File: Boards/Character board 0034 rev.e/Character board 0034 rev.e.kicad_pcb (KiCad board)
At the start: 2 copper layers, 166.4 x 186.7 mm, 40 parts, among them J1 card edge, J2 character connector, J3 power jumper, J4 return jumper, Q1 TIP130A, U1 2.2K, U11 ULN2003A, U12 ULN2003A, U13 7406, U2 2.2K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

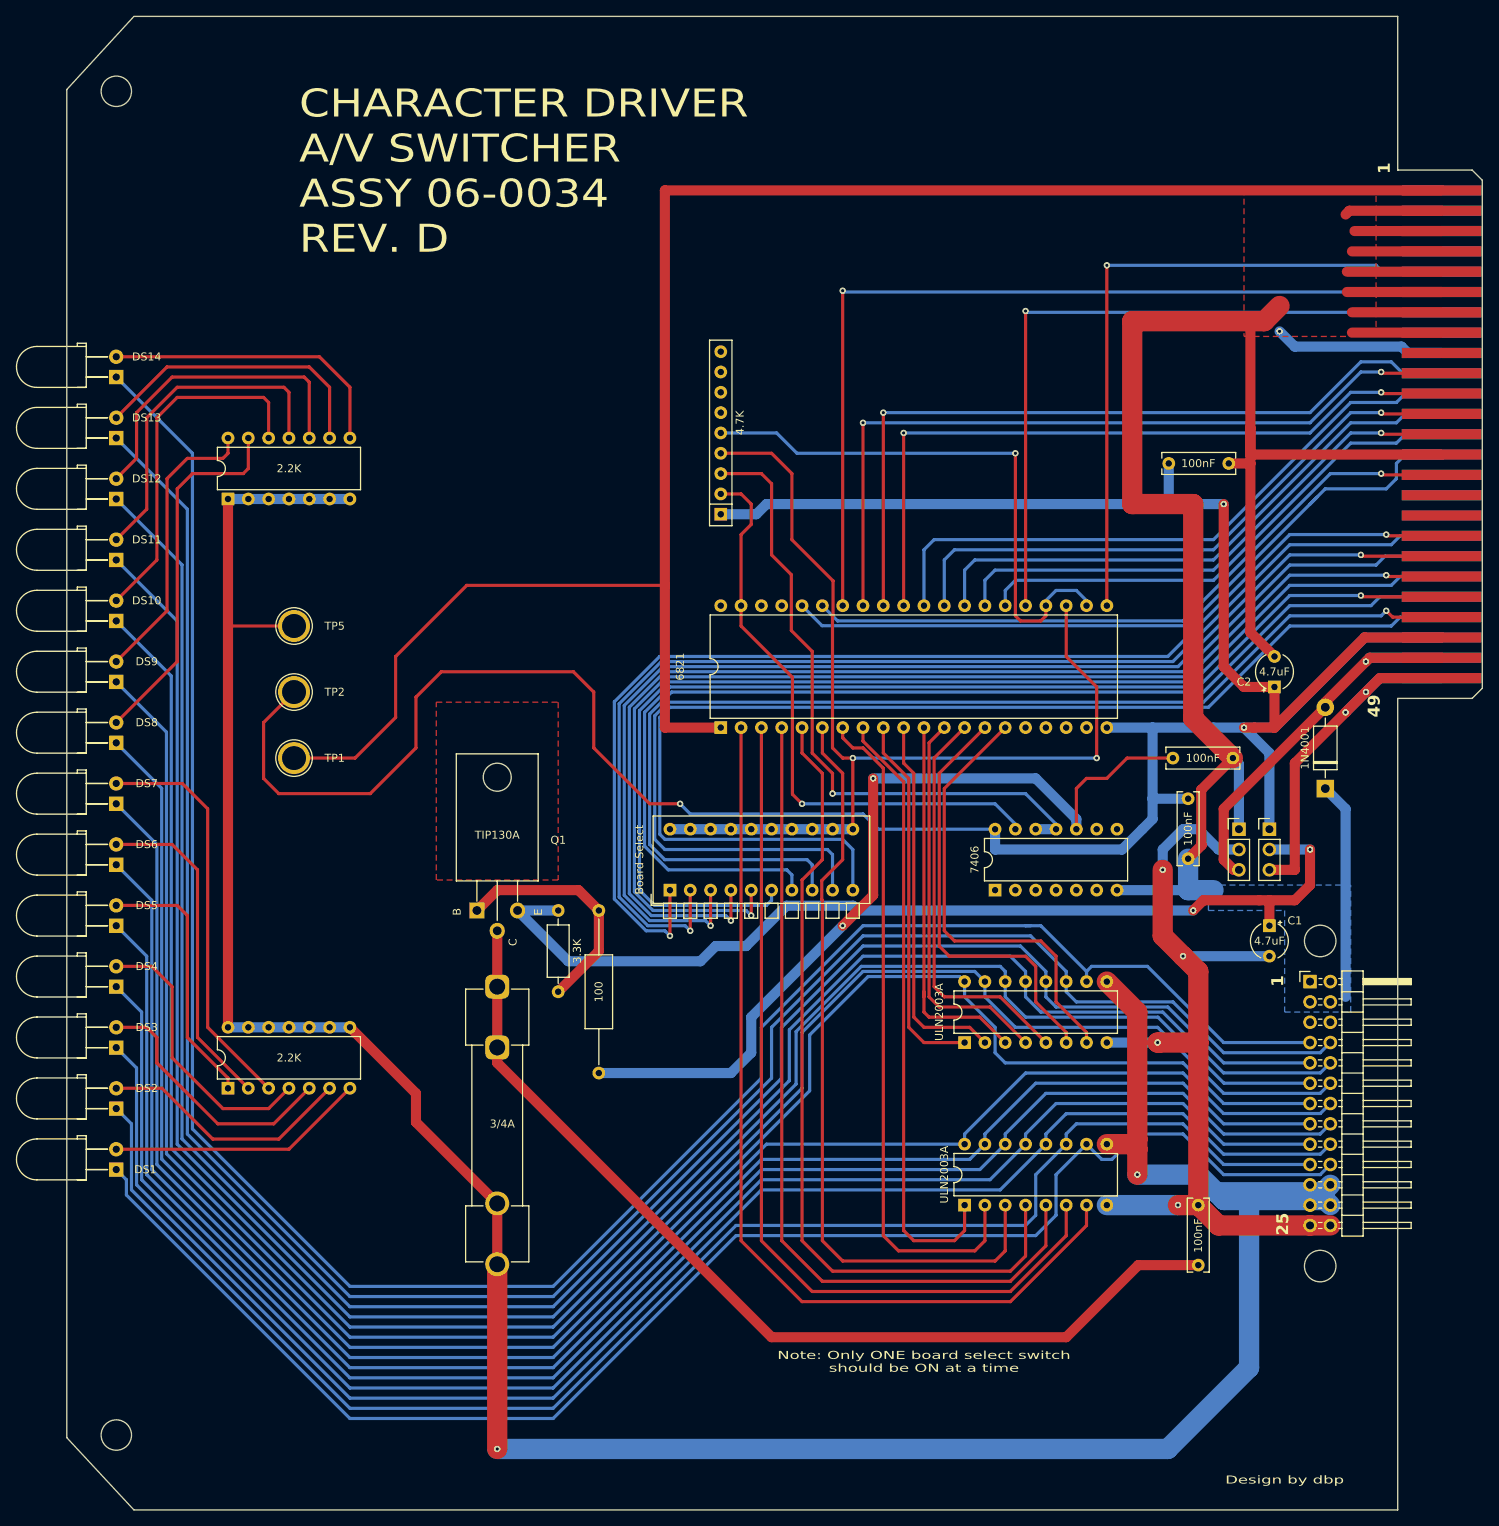
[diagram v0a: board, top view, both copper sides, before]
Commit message: renamed files and started the light card
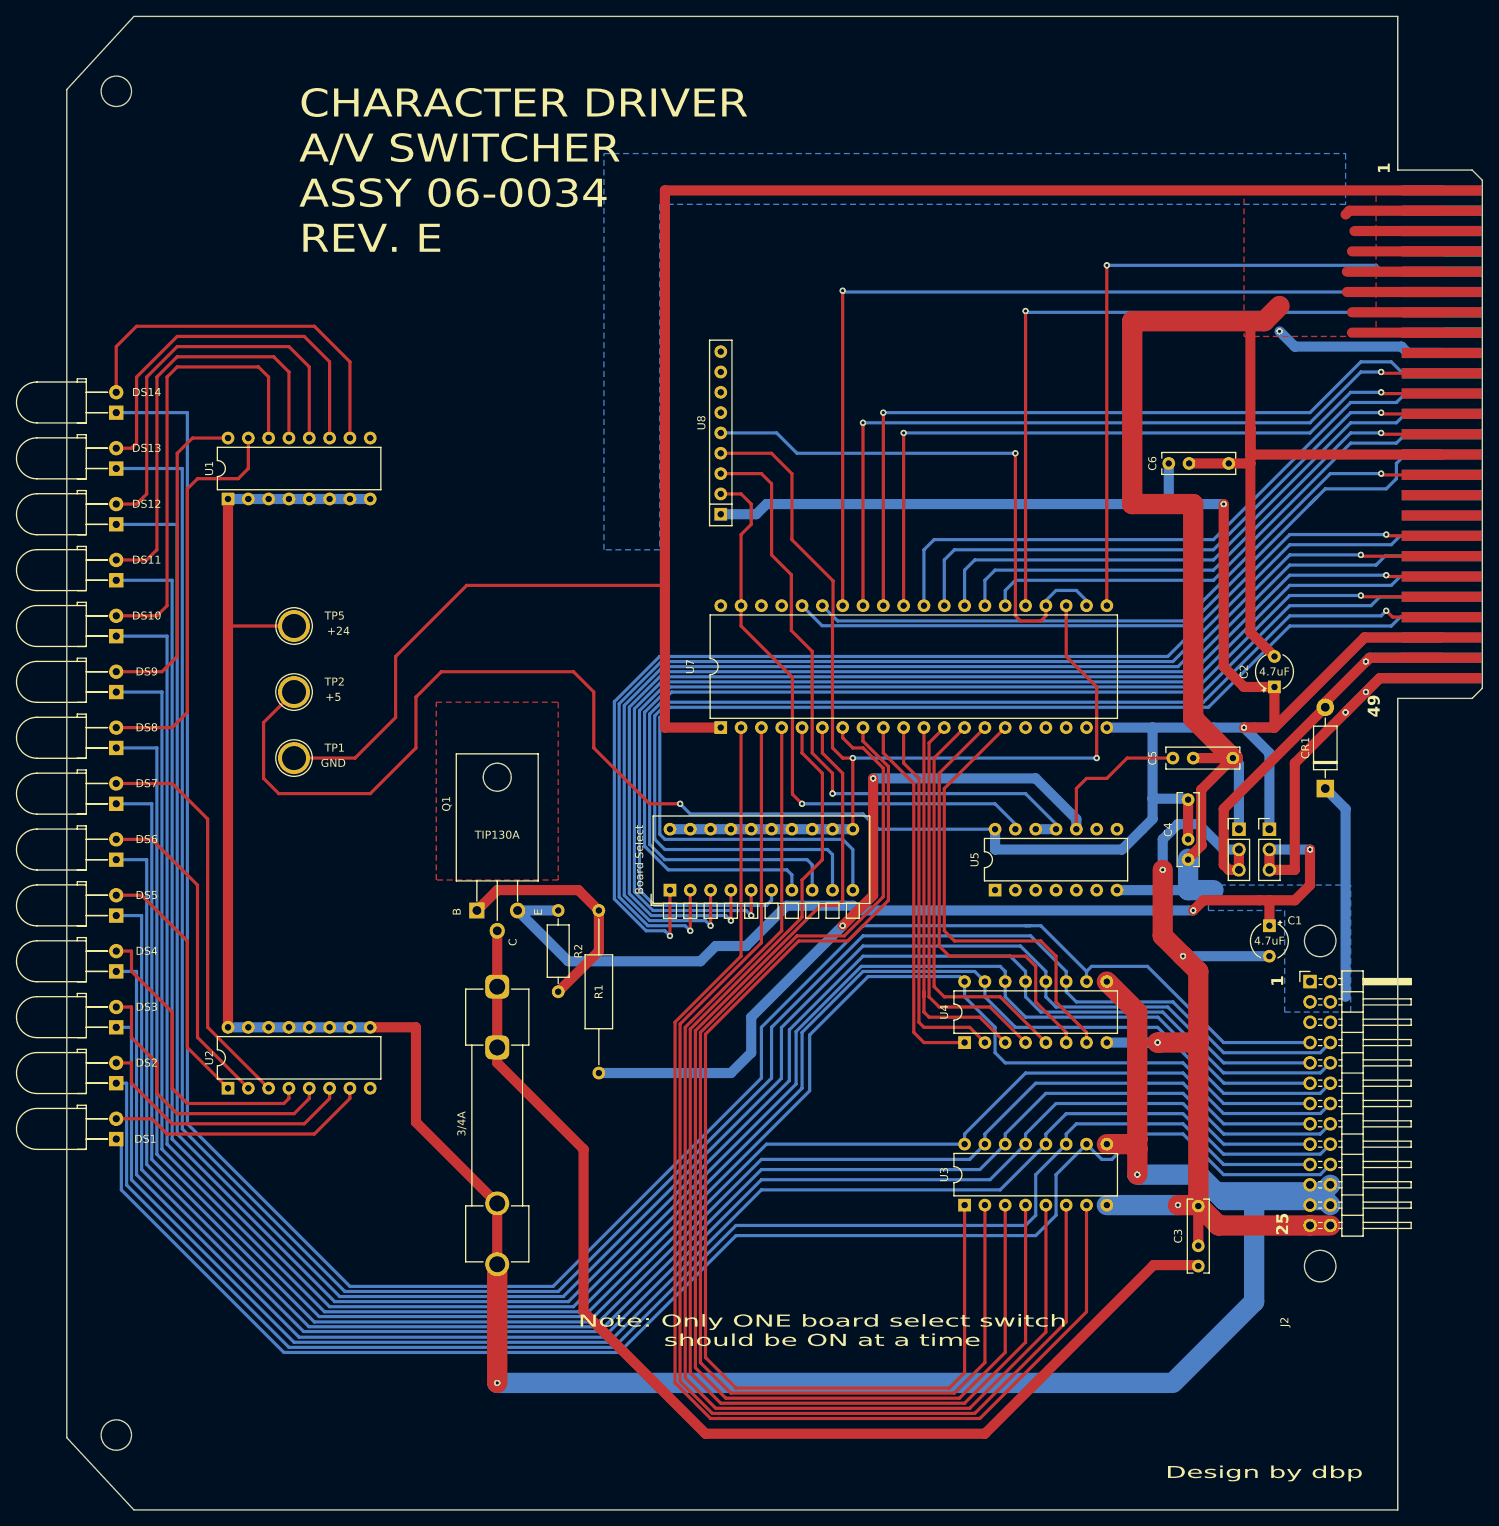
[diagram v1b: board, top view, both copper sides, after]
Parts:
- C3: renamed from C5; footprint Capacitor_THT:C_Rect_L9.0mm_W2.5mm_P7.50mm_MKT -> Evan's parts:C_Rect_L9.0mm_W2.5mm_P7.50mm_MKT dual
- C4: renamed from C10; footprint Capacitor_THT:C_Rect_L9.0mm_W2.5mm_P7.50mm_MKT -> Evan's parts:C_Rect_L9.0mm_W2.5mm_P7.50mm_MKT dual
- C5: renamed from C11; footprint Capacitor_THT:C_Rect_L9.0mm_W2.5mm_P7.50mm_MKT -> Evan's parts:C_Rect_L9.0mm_W2.5mm_P7.50mm_MKT dual
- C6: renamed from C9; footprint Capacitor_THT:C_Rect_L9.0mm_W2.5mm_P7.50mm_MKT -> Evan's parts:C_Rect_L9.0mm_W2.5mm_P7.50mm_MKT dual
- R1: value 100 -> 1K
- TP5: value 24 -> +24
- U1, U2: footprint Package_DIP:DIP-14_W7.62mm -> Package_DIP:DIP-16_W7.62mm
- moved U1 73.7 mm to (38.1, 60.3)
- moved U2 73.7 mm to (38.1, 134.0)
- moved C3 7.62 mm to (159.4, 156.2), turned to 90 degrees
- moved C4 7.62 mm to (158.1, 105.4), turned to 90 degrees
- moved DS14 4.45 mm to (24.1, 47.0)
- moved DS1 3.81 mm to (24.1, 137.8)
- moved DS13 3.81 mm to (24.1, 54.0)
- moved DS2 3.18 mm to (24.1, 130.8)
- moved DS12 3.18 mm to (24.1, 61.0)
- moved DS11 2.54 mm to (24.1, 67.9)
- moved DS3 2.54 mm to (24.1, 123.8)
- moved DS10 1.91 mm to (24.1, 74.9)
- moved DS4 1.91 mm to (24.1, 116.8)
- moved DS9 1.27 mm to (24.1, 81.9)
- moved DS5 1.27 mm to (24.1, 109.9)
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- renumbered R14 to R2, U11 to U3, U12 to U4, U13 to U5, RN1 to U8
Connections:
- C1 pad 1: Net-(J3-Pin_2) -> 24V
- C1 pad 2: return out -> 24R
- C3 pad 1: return out -> Net-(Q1-C)
- C3 pad 2: Net-(Q1-C) -> 24R
- C4 pad 1: 5V -> GND
- C4 pad 2: GND -> 5V
- J2 pad 25: return out -> 24R
- J2 pad 26: return out -> 24R
- J3 pad 2: Net-(J3-Pin_2) -> 24V
- J4 pad 2: return out -> 24R
- Q1 pad 3: Net-(J3-Pin_2) -> 24V
- R2 pad 2: Net-(J3-Pin_2) -> 24V
- U1 pad 1: Net-(DS5-A) -> 24Vout
- U1 pad 10: 24Vout -> Net-(DS14-A)
- U1 pad 11: 24Vout -> Net-(DS13-A)
- U1 pad 12: 24Vout -> Net-(DS12-A)
- U1 pad 13: 24Vout -> Net-(DS11-A)
- U1 pad 14: 24Vout -> Net-(DS10-A)
- U1 pad 2: Net-(DS6-A) -> 24Vout
- U1 pad 3: Net-(DS7-A) -> 24Vout
- U1 pad 4: Net-(DS4-A) -> 24Vout
- U1 pad 5: Net-(DS3-A) -> 24Vout
- U1 pad 6: Net-(DS2-A) -> 24Vout
- U1 pad 7: Net-(DS1-A) -> 24Vout
- U1 pad 9: 24Vout -> unconnected-(U1-R8.2-Pad9)
- U2 pad 1: 24Vout -> Net-(DS5-A)
- U2 pad 10: Net-(DS12-A) -> 24Vout
- U2 pad 11: Net-(DS11-A) -> 24Vout
- U2 pad 12: Net-(DS10-A) -> 24Vout
- U2 pad 13: Net-(DS8-A) -> 24Vout
- U2 pad 14: Net-(DS9-A) -> 24Vout
- U2 pad 2: 24Vout -> Net-(DS6-A)
- U2 pad 3: 24Vout -> Net-(DS7-A)
- U2 pad 4: 24Vout -> Net-(DS4-A)
- U2 pad 5: 24Vout -> Net-(DS3-A)
- U2 pad 6: 24Vout -> Net-(DS2-A)
- U2 pad 7: 24Vout -> Net-(DS1-A)
- U2 pad 8: Net-(DS14-A) -> unconnected-(U2-R8.1-Pad8)
- U2 pad 9: Net-(DS13-A) -> 24Vout
- U3 pad 8: return out -> 24R
- U4 pad 8: return out -> 24R
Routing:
- net 24V: track 53.1 -> 179.5 mm, vias 2 -> 4
- net Net-(J3-Pin_2): track 123.9 -> 0.00 mm, vias 2 -> 0
- net 24R: track 53.9 -> 172.4 mm, vias 1 -> 5
- net return out: track 109.3 -> 0.00 mm, vias 4 -> 0
- net PA6: track 76.8 -> 148.8 mm
- net PA5: track 84.8 -> 153.5 mm
- net PA4: track 96.4 -> 151.0 mm
- net PA3: track 102.9 -> 152.3 mm
- net PA2: track 106.2 -> 152.8 mm
- net PA1: track 111.6 -> 155.2 mm
- net PA0: track 117.0 -> 157.5 mm
- net Net-(Q1-C): track 122.1 -> 144.0 mm
- net Net-(DS10-A): track 44.7 -> 56.8 mm
- net Net-(DS11-A): track 42.2 -> 53.8 mm
- net Net-(DS13-A): track 36.7 -> 48.1 mm
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- added copper zone on B.Cu, net (none)
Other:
- board text added: "CHARACTER DRIVER A/V SWITCHER ASSY 06-0034 REV. E"
- board text removed: "CHARACTER DRIVER A/V SWITCHER ASSY 06-0034 REV. D"

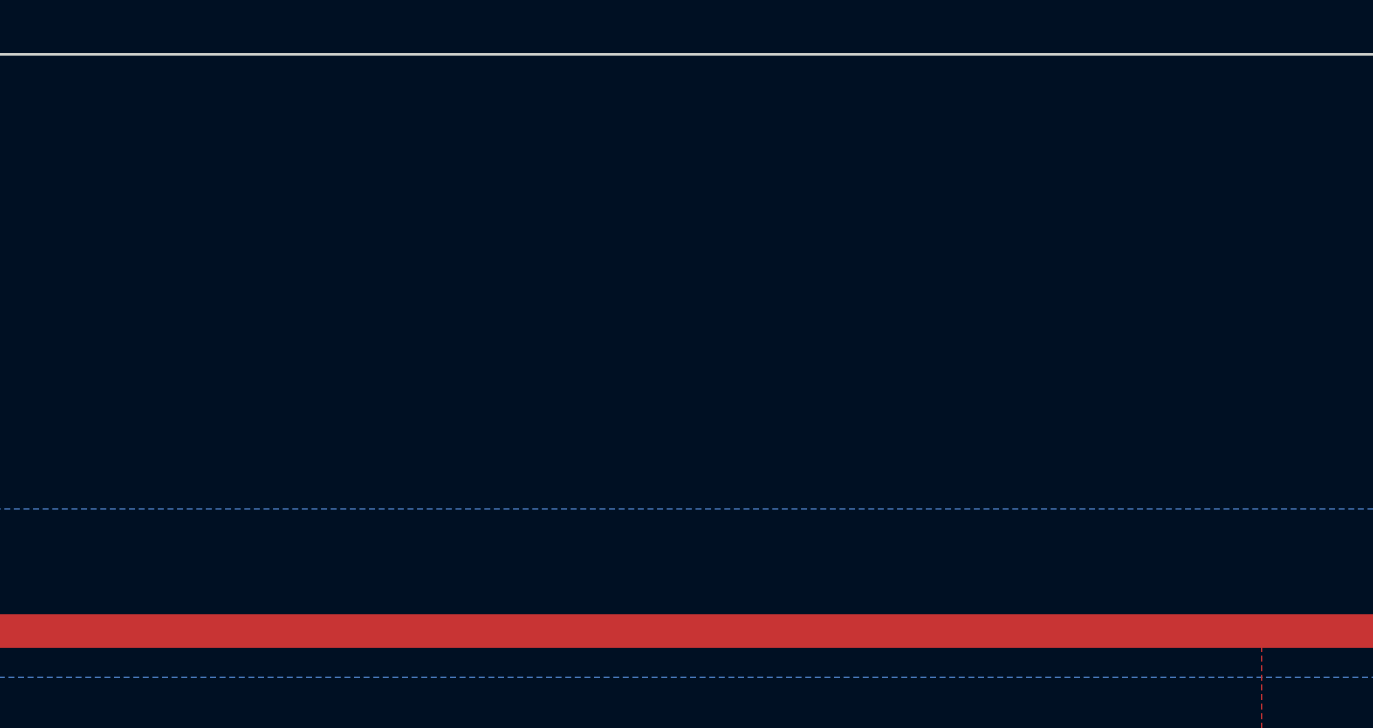
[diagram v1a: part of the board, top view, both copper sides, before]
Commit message: added logos
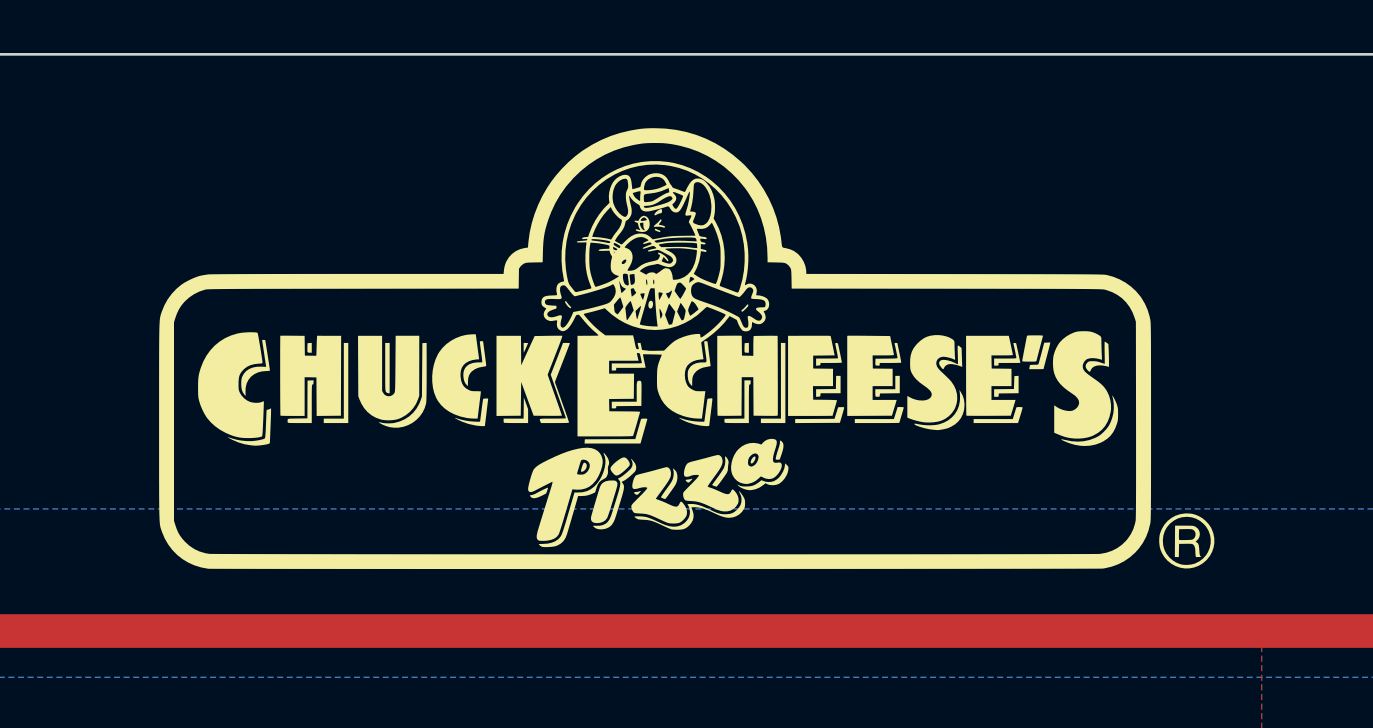
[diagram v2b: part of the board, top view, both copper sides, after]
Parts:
- added G***: LOGO, Evan's parts:pizza logo, F.Cu at (143.5, 13.3)
